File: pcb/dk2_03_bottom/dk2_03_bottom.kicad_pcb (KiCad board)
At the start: 2 copper layers, 120 x 80 mm, 76 parts, among them J1 Conn_01x18_Pin, J2 Conn_01x18_Pin, J3 Eurorack_Power, Q1 MMBT3904, U1 Pico, U2 AP7333-33SRG, U3 TL072, U4 PCM5102, U5 TL072, U6 TL072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

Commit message: getting ready for next PCBs
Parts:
- removed H1, H2, H3, H4: MountingHole, MountingHole:MountingHole_3.2mm_M3
- U2: value AP7333-33SRG -> AP7333-33SAG
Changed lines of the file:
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@@
     (descr "SOD-323")
     (tags "SOD-323")
-    (property "Sheetfile" "dk2_02_bottom.kicad_sch")
+    (property "Sheetfile" "dk2_03_bottom.kicad_sch")
     (property "Sheetname" "")
     (property "ki_description" "40V 600mV@1A 1A SOD-323 Schottky Barrier Diodes, SOD-323")
@@
     )
   )
-  (footprint "MountingHole:MountingHole_3.2mm_M3" (layer "F.Cu")
-    (at 196 126)
-    (descr "Mounting Hole 3.2mm, no annular, M3")
-    (tags "mounting hole 3.2mm no annular m3")
-    (property "Sheetfile" "dk2_02_bottom.kicad_sch")
-    (property "Sheetname" "")
-    (property "ki_description" "Mounting Hole without connection")
-    (property "ki_keywords" "mounting hole")
-    (attr exclude_from_pos_files)
-    (fp_text reference "H4" (at 0 -4.2) (layer "F.SilkS")
-        (effects (font (size 1 1) (thickness 0.15)))
-    )
-    (fp_text value "MountingHole" (at 0 4.2) (layer "F.Fab")
-        (effects (font (size 1 1) (thickness 0.15)))
-    )
-    (fp_text user "${REFERENCE}" (at 0 0) (layer "F.Fab")
-        (effects (font (size 1 1) (thickness 0.15)))
-    )
-    (fp_circle (center 0 0) (end 3.2 0)
-      (stroke (width 0.15) (type solid)) (fill none) (layer "Cmts.User"))
-    (fp_circle (center 0 0) (end 3.45 0)
-      (stroke (width 0.05) (type solid)) (fill none) (layer "F.CrtYd"))
-    (pad "" np_thru_hole circle (at 0 0) (size 3.2 3.2) (drill 3.2) (layers "*.Cu" "*.Mask"))
-  )
   (footprint "Resistor_SMD:R_0603_1608Metric" (layer "F.Cu")
     (at 180.325 106.6)
@@
     )
   )
-  (footprint "MountingHole:MountingHole_3.2mm_M3" (layer "F.Cu")
-    (at 84 126)
-    (descr "Mounting Hole 3.2mm, no annular, M3")
-    (tags "mounting hole 3.2mm no annular m3")
-    (property "Sheetfile" "dk2_02_bottom.kicad_sch")
-    (property "Sheetname" "")
-    (property "ki_description" "Mounting Hole without connection")
-    (property "ki_keywords" "mounting hole")
-    (attr exclude_from_pos_files)
-    (fp_text reference "H3" (at 0 -4.2) (layer "F.SilkS")
-        (effects (font (size 1 1) (thickness 0.15)))
-    )
-    (fp_text value "MountingHole" (at 0 4.2) (layer "F.Fab")
-        (effects (font (size 1 1) (thickness 0.15)))
-    )
-    (fp_text user "${REFERENCE}" (at 0 0) (layer "F.Fab")
-        (effects (font (size 1 1) (thickness 0.15)))
-    )
-    (fp_circle (center 0 0) (end 3.2 0)
-      (stroke (width 0.15) (type solid)) (fill none) (layer "Cmts.User"))
-    (fp_circle (center 0 0) (end 3.45 0)
-      (stroke (width 0.05) (type solid)) (fill none) (layer "F.CrtYd"))
-    (pad "" np_thru_hole circle (at 0 0) (size 3.2 3.2) (drill 3.2) (layers "*.Cu" "*.Mask"))
-  )
   (footprint "Capacitor_SMD:C_0603_1608Metric" (layer "F.Cu")
     (at 108.1 101.935 180)
@@
     )
   )
-  (footprint "MountingHole:MountingHole_3.2mm_M3" (layer "F.Cu")
-    (at 196 54 180)
-    (descr "Mounting Hole 3.2mm, no annular, M3")
-    (tags "mounting hole 3.2mm no annular m3")
-    (property "Sheetfile" "dk2_02_bottom.kicad_sch")
-    (property "Sheetname" "")
-    (property "ki_description" "Mounting Hole without connection")
-    (property "ki_keywords" "mounting hole")
-    (attr exclude_from_pos_files)
-    (fp_text reference "H2" (at 0 -4.2) (layer "F.SilkS")
-        (effects (font (size 1 1) (thickness 0.15)))
-    )
-    (fp_text value "MountingHole" (at 0 4.2) (layer "F.Fab")
-        (effects (font (size 1 1) (thickness 0.15)))
-    )
-    (fp_text user "${REFERENCE}" (at 0 0) (layer "F.Fab")
-        (effects (font (size 1 1) (thickness 0.15)))
-    )
-    (fp_circle (center 0 0) (end 3.2 0)
-      (stroke (width 0.15) (type solid)) (fill none) (layer "Cmts.User"))
-    (fp_circle (center 0 0) (end 3.45 0)
-      (stroke (width 0.05) (type solid)) (fill none) (layer "F.CrtYd"))
-    (pad "" np_thru_hole circle (at 0 0 180) (size 3.2 3.2) (drill 3.2) (layers "*.Cu" "*.Mask"))
-  )
   (footprint "Resistor_SMD:R_0603_1608Metric" (layer "F.Cu")
     (at 113.5 88.535)
@@
     (descr "Through hole straight pin header, 1x18, 2.54mm pitch, single row")
     (tags "Through hole pin header THT 1x18 2.54mm single row")
-    (property "Sheetfile" "dk2_02_bottom.kicad_sch")
+    (property "Sheetfile" "dk2_03_bottom.kicad_sch")
     (property "Sheetname" "")
     (property "ki_description" "Generic connector, single row, 01x18, script generated")
@@
     )
   )
-  (footprint "MountingHole:MountingHole_3.2mm_M3" (layer "F.Cu")
-    (at 84 54 180)
-    (descr "Mounting Hole 3.2mm, no annular, M3")
-    (tags "mounting hole 3.2mm no annular m3")
-    (property "Sheetfile" "dk2_02_bottom.kicad_sch")
-    (property "Sheetname" "")
-    (property "ki_description" "Mounting Hole without connection")
-    (property "ki_keywords" "mounting hole")
-    (attr exclude_from_pos_files)
-    (fp_text reference "H1" (at 0 -4.2) (layer "F.SilkS")
-        (effects (font (size 1 1) (thickness 0.15)))
-    )
-    (fp_text value "MountingHole" (at 0 4.2) (layer "F.Fab")
-        (effects (font (size 1 1) (thickness 0.15)))
-    )
-    (fp_text user "${REFERENCE}" (at 0 0) (layer "F.Fab")
-        (effects (font (size 1 1) (thickness 0.15)))
-    )
-    (fp_circle (center 0 0) (end 3.2 0)
-      (stroke (width 0.15) (type solid)) (fill none) (layer "Cmts.User"))
-    (fp_circle (center 0 0) (end 3.45 0)
-      (stroke (width 0.05) (type solid)) (fill none) (layer "F.CrtYd"))
-    (pad "" np_thru_hole circle (at 0 0 180) (size 3.2 3.2) (drill 3.2) (layers "*.Cu" "*.Mask"))
-  )
   (footprint "Connector_PinHeader_2.54mm:PinHeader_1x18_P2.54mm_Vertical" (layer "F.Cu")
     (at 196 76.82)
     (descr "Through hole straight pin header, 1x18, 2.54mm pitch, single row")
     (tags "Through hole pin header THT 1x18 2.54mm single row")
-    (property "Sheetfile" "dk2_02_bottom.kicad_sch")
+    (property "Sheetfile" "dk2_03_bottom.kicad_sch")
     (property "Sheetname" "")
     (property "ki_description" "Generic connector, single row, 01x18, script generated")
@@
         (effects (font (size 1 1) (thickness 0.15)))
     )
-    (fp_text value "AP7333-33SRG" (at 0 2.4) (layer "F.Fab")
+    (fp_text value "AP7333-33SAG" (at 0 2.4) (layer "F.Fab")
         (effects (font (size 1 1) (thickness 0.15)))
     )
@@
     (descr "Through hole straight pin header, 2x20, 2.54mm pitch, double rows")
     (tags "Through hole pin header THT 2x20 2.54mm double row")
-    (property "Sheetfile" "dk2_02_bottom.kicad_sch")
+    (property "Sheetfile" "dk2_03_bottom.kicad_sch")
     (property "Sheetname" "")
     (attr through_hole)

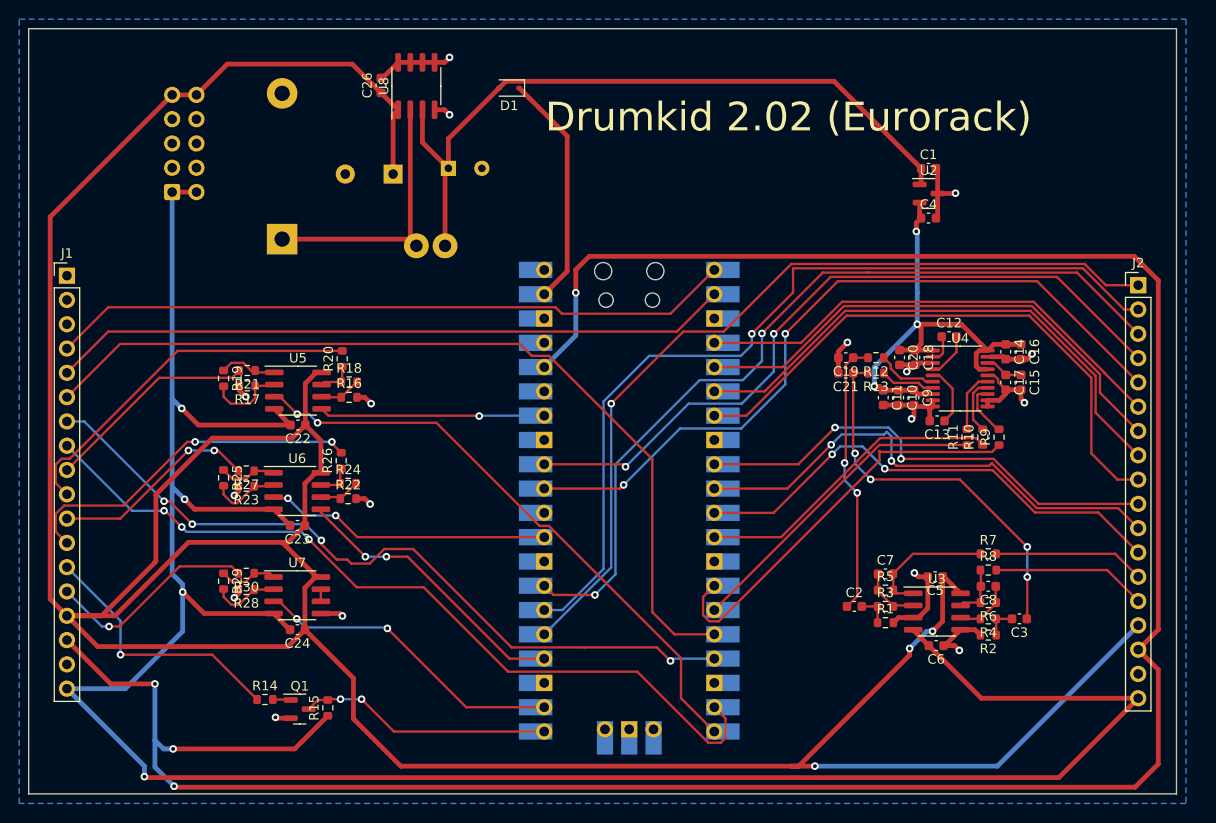
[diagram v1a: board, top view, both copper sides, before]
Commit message: bottom pcb shrunk
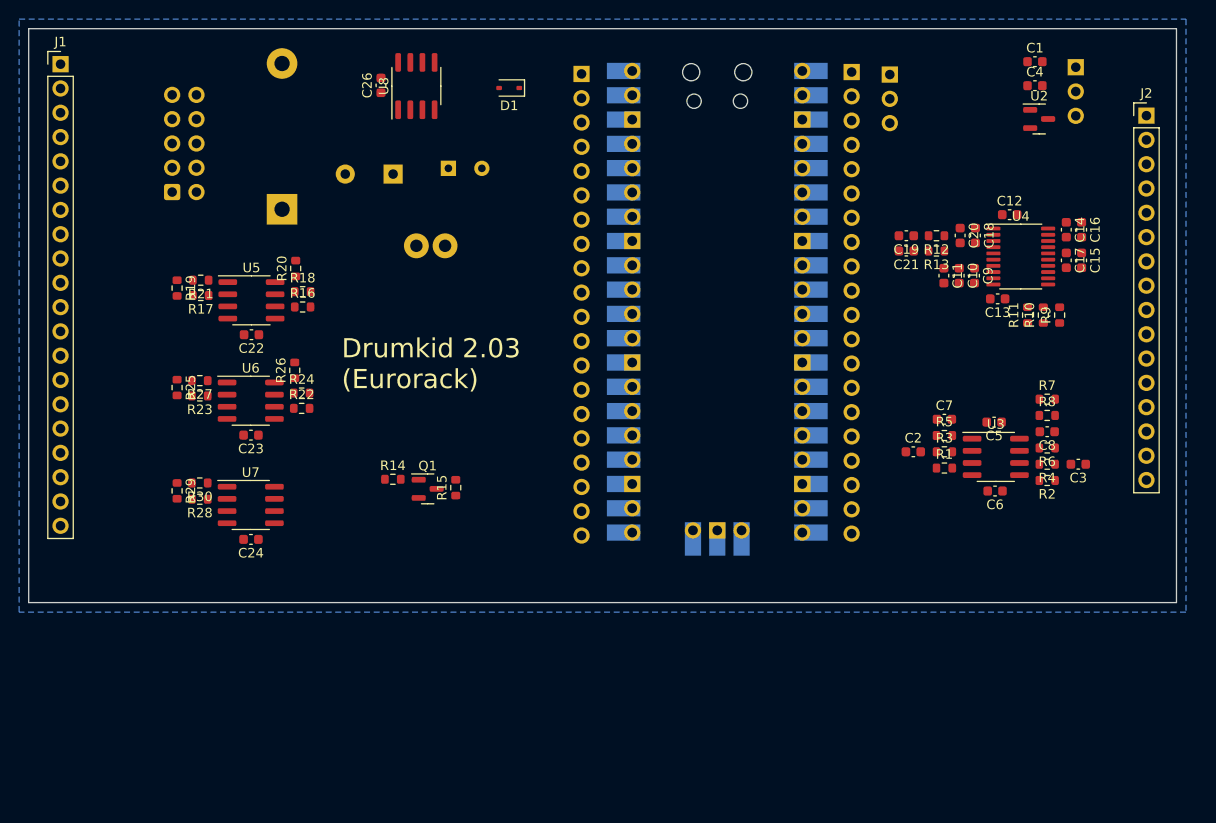
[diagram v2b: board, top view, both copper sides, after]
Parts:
- added J4: Conn_01x20_Pin, Connector_PinHeader_2.54mm:PinHeader_1x20_P2.54mm_Vertical, B.Cu at (166.0, 54.5)
- added J5: Conn_01x20_Pin, Connector_PinHeader_2.54mm:PinHeader_1x20_P2.54mm_Vertical, B.Cu at (137.8, 54.7)
- added J6: Conn_01x03_Pin, Connector_PinHeader_2.54mm:PinHeader_1x03_P2.54mm_Vertical, B.Cu at (170.0, 54.8)
- added JP1: Jumper_3_Open, Connector_PinHeader_2.54mm:PinHeader_1x03_P2.54mm_Vertical, B.Cu at (189.5, 54.0)
- J1: value Conn_01x18_Pin -> Conn_01x20_Pin; footprint Connector_PinHeader_2.54mm:PinHeader_1x18_P2.54mm_Vertical -> Connector_PinHeader_2.54mm:PinHeader_1x20_P2.54mm_Vertical
- J2: value Conn_01x18_Pin -> Conn_01x16_Pin; footprint Connector_PinHeader_2.54mm:PinHeader_1x18_P2.54mm_Vertical -> Connector_PinHeader_2.54mm:PinHeader_1x16_P2.54mm_Vertical
- moved Q1 26.6 mm to (121.7, 98.1)
- moved R14 26.6 mm to (118.1, 97.1)
- moved R15 26.6 mm to (124.7, 98.0)
- moved U1 22.7 mm to (152.0, 78.5)
- moved J1 22.1 mm to (83.3, 53.7)
- moved C4 17.8 mm to (185.2, 56.0)
- moved J2 17.8 mm to (196.9, 59.1)
- moved C2 17.3 mm to (172.5, 94.2)
- moved C3 17.3 mm to (189.7, 95.5)
- moved C7 17.3 mm to (175.7, 90.8)
- moved R2 17.3 mm to (186.5, 97.2)
- moved R3 17.3 mm to (175.7, 94.2)
- moved R4 17.3 mm to (186.5, 95.5)
- moved R5 17.3 mm to (175.7, 92.5)
- moved R6 17.3 mm to (186.5, 93.8)
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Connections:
- C4 pad 1: +3.3VDAC -> Net-(JP1-A)
- J1 pad 10: TRIGGER_OUT_2_EURO -> TRIGGER_OUT_1_EURO
- J1 pad 11: TRIGGER_OUT_3_EURO -> TRIGGER_OUT_2_EURO
- J1 pad 12: TRIGGER_OUT_4_EURO -> TRIGGER_OUT_3_EURO
- J1 pad 13: SYNC_IN_EURO -> TRIGGER_OUT_4_EURO
- J1 pad 14: SYNC_OUT_EURO -> SYNC_IN_EURO
- J1 pad 15: +12V -> SYNC_OUT_EURO
- J1 pad 16: +3.3V -> +12V
- J1 pad 17: GND -> +3.3VDAC
- J1 pad 18: -12V -> +3.3V
- J1 pad 2: unconnected-(J1-Pin_2-Pad2) -> 4051_ADDRESS_A
- J1 pad 3: unconnected-(J1-Pin_3-Pad3) -> 4051_ADDRESS_B
- J1 pad 4: START_STOP_BUTTON -> 4051_ADDRESS_C
- J1 pad 5: TAP_TEMPO_BUTTON -> 4051_READING_1
- J1 pad 6: 165_LOAD -> 4051_READING_0
- J1 pad 7: 165_CLOCK -> 165_LOAD
- J1 pad 8: 165_DATA -> 165_CLOCK
- J1 pad 9: TRIGGER_OUT_1_EURO -> 165_DATA
- J2 pad 1: 4051_ADDRESS_A -> unconnected-(J2-Pin_1-Pad1)
- J2 pad 10: 595_DATA -> EURO_OUT_1
- J2 pad 11: 595_CLOCK -> EURO_OUT_2
- J2 pad 12: 595_LATCH -> +12V
- J2 pad 13: EURO_OUT_1 -> +3.3VDAC
- J2 pad 14: EURO_OUT_2 -> +3.3V
- J2 pad 15: +12V -> GND
- J2 pad 16: +3.3V -> -12V
- J2 pad 2: 4051_ADDRESS_B -> unconnected-(J2-Pin_2-Pad2)
- J2 pad 3: 4051_ADDRESS_C -> SD_CLOCK
- J2 pad 4: 4051_READING_1 -> SD_SERIAL_IN
- J2 pad 5: 4051_READING_0 -> SD_SERIAL_OUT
- J2 pad 6: SD_CLOCK -> SD_CHIP_SELECT
- J2 pad 7: SD_SERIAL_IN -> 595_DATA
- J2 pad 8: SD_SERIAL_OUT -> 595_CLOCK
- J2 pad 9: SD_CHIP_SELECT -> 595_LATCH
- U1 pad 1: START_STOP_BUTTON -> SERIAL_TX
- U1 pad 2: TAP_TEMPO_BUTTON -> SERIAL_RX
- U2 pad 2: +3.3VDAC -> Net-(JP1-A)
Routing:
- net +12V: track 349.6 -> 0.00 mm, vias 3 -> 0
- net +3.3V: track 272.8 -> 0.00 mm, vias 4 -> 0
- net -12V: track 252.8 -> 0.00 mm, vias 4 -> 0
- net 165_LOAD: track 91.9 -> 0.00 mm
- net 4051_ADDRESS_B: track 91.1 -> 0.00 mm, vias 1 -> 0
- net 4051_ADDRESS_A: track 89.1 -> 0.00 mm, vias 1 -> 0
- net 4051_ADDRESS_C: track 87.5 -> 0.00 mm, vias 2 -> 0
- net 165_DATA: track 85.6 -> 0.00 mm, vias 3 -> 0
- net 165_CLOCK: track 79.6 -> 0.00 mm, vias 4 -> 0
- net 4051_READING_0: track 78.6 -> 0.00 mm, vias 2 -> 0
- net 4051_READING_1: track 76.3 -> 0.00 mm, vias 2 -> 0
- net +5V: track 76.0 -> 0.00 mm
- net GND: track 74.9 -> 0.00 mm, vias 17 -> 0
- net START_STOP_BUTTON: track 71.6 -> 0.00 mm
- net TAP_TEMPO_BUTTON: track 71.1 -> 0.00 mm
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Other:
- board size 120 x 80 mm -> 120 x 60 mm
- board text added: "Drumkid 2.03 (Eurorack)"
- board text removed: "Drumkid 2.02 (Eurorack)"

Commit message: a commit before i mess up all the buttons
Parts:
- moved J2 2.27 mm to (195.6, 61.0)
- moved J1 2.22 mm to (83.8, 55.9)
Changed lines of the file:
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@@
   )
   (footprint "Connector_PinHeader_2.54mm:PinHeader_1x20_P2.54mm_Vertical" (layer "F.Cu")
-    (at 83.33 53.71)
+    (at 83.82 55.88)
     (descr "Through hole straight pin header, 1x20, 2.54mm pitch, single row")
     (tags "Through hole pin header THT 1x20 2.54mm single row")
@@
   )
   (footprint "Connector_PinHeader_2.54mm:PinHeader_1x16_P2.54mm_Vertical" (layer "F.Cu")
-    (at 196.86 59.09)
+    (at 195.58 60.96)
     (descr "Through hole straight pin header, 1x16, 2.54mm pitch, single row")
     (tags "Through hole pin header THT 1x16 2.54mm single row")

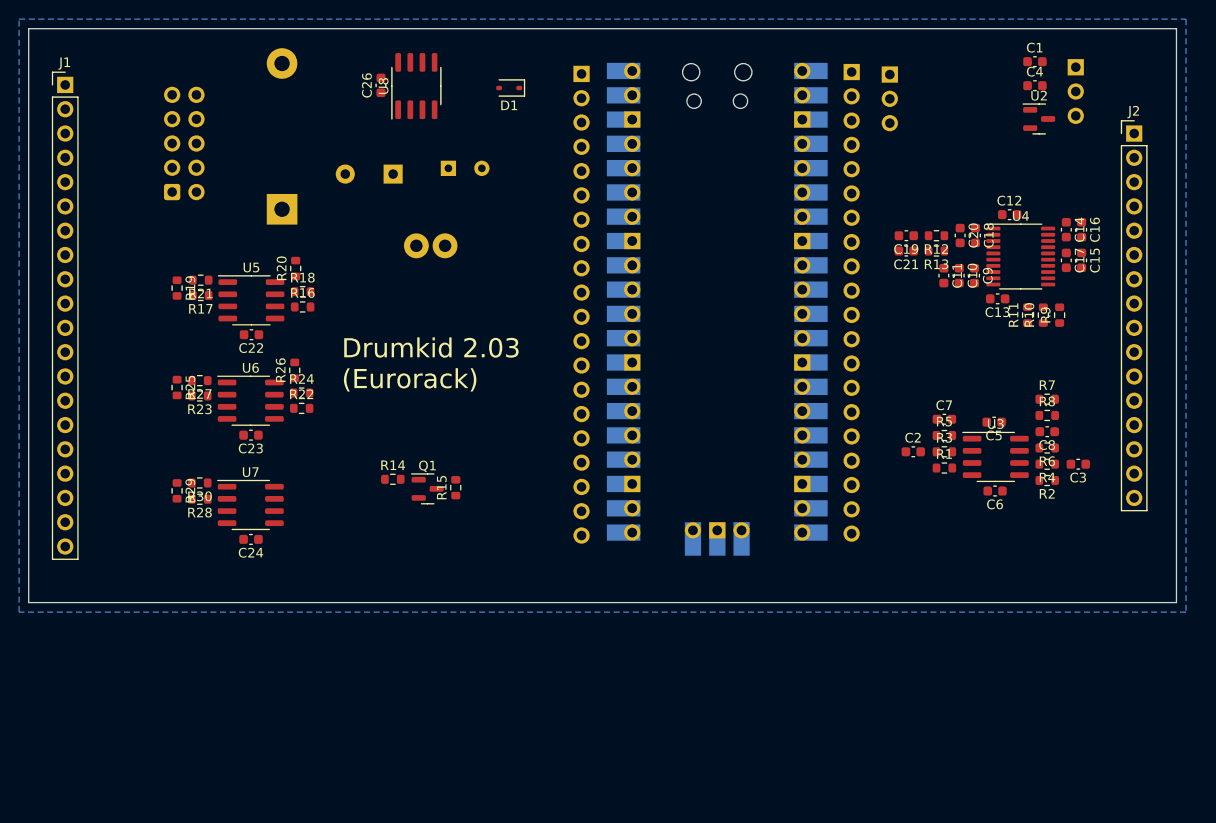
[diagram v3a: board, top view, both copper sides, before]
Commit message: routing bottom pcb
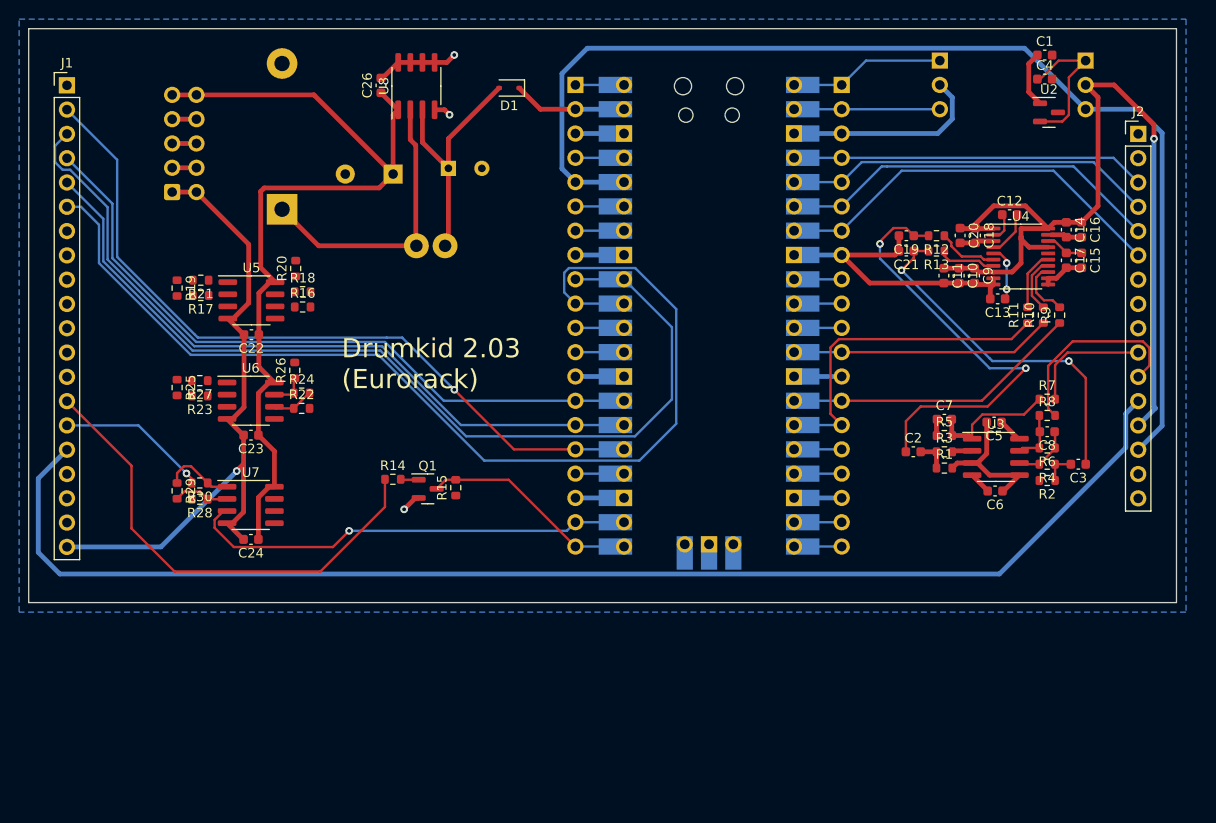
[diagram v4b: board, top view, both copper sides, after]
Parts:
- moved J6 5.43 mm to (175.3, 53.3)
- moved J4 1.70 mm to (165.0, 55.9)
- moved U1 1.69 mm to (151.1, 80.0)
- moved J5 1.32 mm to (137.2, 55.9)
- moved C1 1.24 mm to (186.2, 52.8)
- moved C4 1.24 mm to (186.2, 55.3)
- moved JP1 1.24 mm to (190.5, 53.3)
- moved U2 1.24 mm to (186.7, 58.8)
- moved J2 0.42 mm to (196.0, 61.0)
- moved J1 0.18 mm to (84.0, 55.9)
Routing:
- net +12V: track 0.00 -> 232.1 mm
- net GND: track 0.00 -> 130.1 mm, vias 0 -> 3
- net +3.3V: track 0.00 -> 118.7 mm
- net 4051_READING_0: track 0.00 -> 113.1 mm
- net 4051_READING_1: track 0.00 -> 98.1 mm
- net +3.3VDAC: track 0.00 -> 92.3 mm, vias 0 -> 1
- net 4051_ADDRESS_A: track 0.00 -> 78.9 mm, vias 0 -> 1
- net 4051_ADDRESS_B: track 0.00 -> 77.5 mm
- net 4051_ADDRESS_C: track 0.00 -> 72.1 mm
- net -12V: track 0.00 -> 71.0 mm, vias 0 -> 1
- net SYNC_IN_EURO: track 0.00 -> 50.2 mm
- net SYNC_OUT: track 0.00 -> 47.2 mm, vias 0 -> 1
- net LINE_OUT_L: track 0.00 -> 45.8 mm, vias 0 -> 2
- net SD_CHIP_SELECT: track 0.00 -> 42.2 mm
- net SD_SERIAL_OUT: track 0.00 -> 40.5 mm
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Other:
- board text added: "AP7333 DAC PICO"
- board text added: "TX GND RX"
